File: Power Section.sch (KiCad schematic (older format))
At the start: 60 parts, among them J17 CK-JS102011SAQN, J4 USB_C_Receptacle_USB2.0, Q1 SSM6J507NU, Q2 SSM6J507NU, Q3 SSM6J507NU, Q6 SSM6J507NU, U1 LM1117LDX, U2 LDFM33PVR, U5 MCP73213, U6 BQ29209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

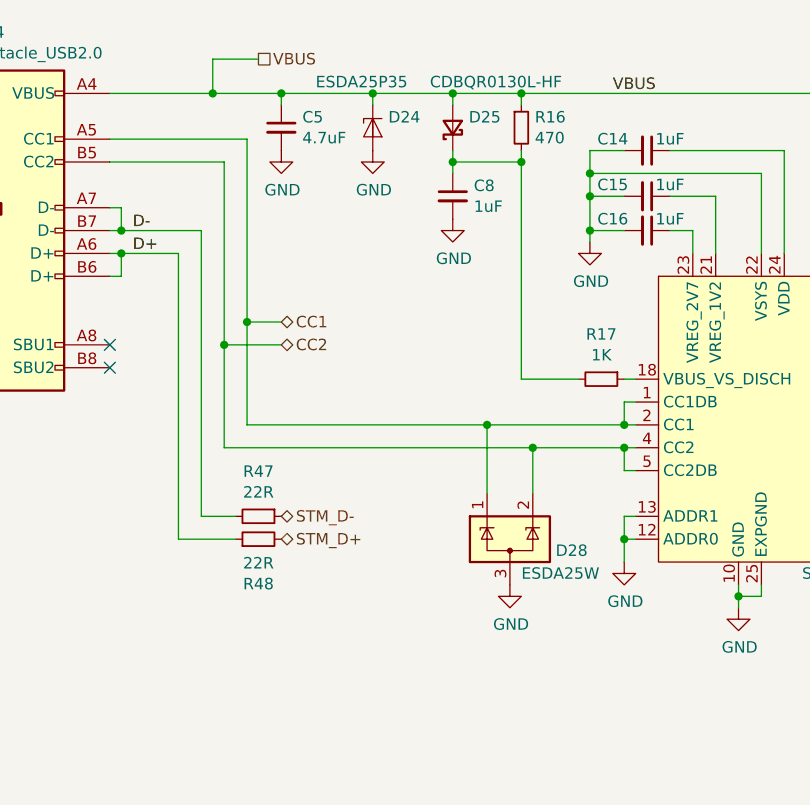
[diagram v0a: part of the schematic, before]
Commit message: Dodano projekt stacji dokującej. Poprawki ścieżek i shcematu
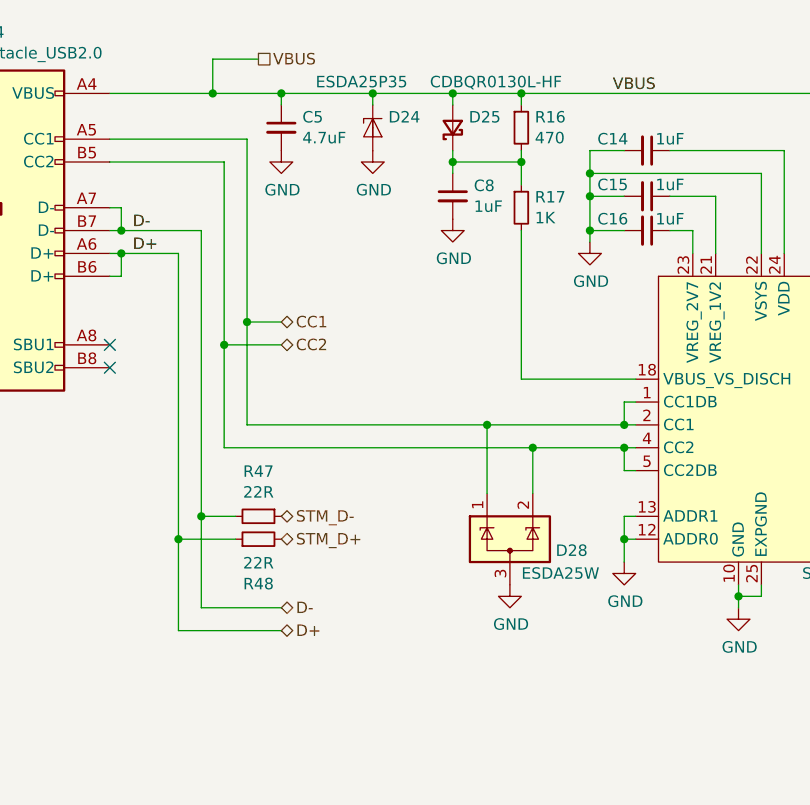
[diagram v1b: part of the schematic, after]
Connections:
- wire segments 228 -> 232
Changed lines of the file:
@@
 Connection ~ 3900 4950
-$Comp
-L Device:R_Small R17
-U 1 1 5FB18F14
-P 3800 4750
-F 0 "R17" V 3604 4750 50  0000 C CNN
-F 1 "1K" V 3695 4750 50  0000 C CNN
-F 2 "Resistor_SMD:R_0402_1005Metric" H 3800 4750 50  0001 C CNN
-F 3 "~" H 3800 4750 50  0001 C CNN
-	1    3800 4750
-	0    1    1    0
-$EndComp
-Wire Wire Line
-	3950 4750 3900 4750
 $Comp
 L Device:C_Small C16
@@
 	1    0    0    -1
 $EndComp
-Wire Wire Line
-	3700 4750 3450 4750
 $Comp
 L Device:D_Schottky_Small D25
@@
 Connection ~ 3450 3800
 Wire Wire Line
-	3450 3800 3450 4750
+	3450 3800 3450 3900
 $Comp
 L synermycha-electronics:ESDA25P35 D24
@@
 Text Label 1750 4200 0    50   ~ 0
 D+
+$Comp
+L Device:R_Small R17
+U 1 1 5FA3A7AB
+P 3450 4000
+F 0 "R17" H 3509 4046 50  0000 L CNN
+F 1 "1K" H 3509 3955 50  0000 L CNN
+F 2 "Resistor_SMD:R_0402_1005Metric" H 3450 4000 50  0001 C CNN
+F 3 "" H 3450 4000 50  0001 C CNN
+	1    3450 4000
+	1    0    0    -1
+$EndComp
+Wire Wire Line
+	3450 4100 3450 4750
+Wire Wire Line
+	3450 4750 3950 4750
+Text HLabel 2400 5750 2    50   BiDi ~ 0
+D-
+Text HLabel 2400 5850 2    50   BiDi ~ 0
+D+
+Wire Wire Line
+	2400 5750 2050 5750
+Wire Wire Line
+	2050 5750 2050 5350
+Connection ~ 2050 5350
+Wire Wire Line
+	2400 5850 1950 5850
+Wire Wire Line
+	1950 5850 1950 5450
+Connection ~ 1950 5450
 $EndSCHEMATC

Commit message: NXP version
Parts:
- removed BT2, BT3, BT4: 200mAh, Connector_PinHeader_1.27mm:PinHeader_1x02_P1.27mm_Vertical, symbol Device:Battery_Cell
- removed C14, C15, C16: 1uF, Capacitor_SMD:C_0402_1005Metric, symbol Device:C_Small
- removed C17, C18, C20, C21: 0.1uF, Capacitor_SMD:C_0402_1005Metric, symbol Device:C_Small
- removed C19: 0.33uF, Capacitor_SMD:C_0402_1005Metric, symbol Device:C_Small
- removed D25: CDBQR0130L-HF, Diode_SMD:D_0402_1005Metric, symbol Device:D_Schottky_Small
- removed D26: RED, LED_SMD:LED_0402_1005Metric, symbol Device:LED_Small
- removed D28: ESDA25W, Package_TO_SOT_SMD:SOT-323_SC-70, symbol synermycha-electronics:ESDA25W
- removed D29: ESDA25P35, footprints:1610, symbol synermycha-electronics:ESDA25P35
- removed Q2: SSM6J507NU, footprints:UDFN6B, symbol synermycha-electronics:SSM6J507NU
- removed R16: 470, Resistor_SMD:R_0402_1005Metric, symbol Device:R_Small
- removed R17: 1K, Resistor_SMD:R_0402_1005Metric, symbol Device:R_Small
- removed R18, R28: 100K, Resistor_SMD:R_0402_1005Metric, symbol Device:R_Small
- removed R21: 18K, Resistor_SMD:R_0402_1005Metric, symbol Device:R_Small
- removed R35: 100R, Resistor_SMD:R_0402_1005Metric, symbol Device:R_Small
- removed R41: 160R, Resistor_SMD:R_0402_1005Metric, symbol Device:R_Small
- removed R44: 260R, Resistor_SMD:R_0402_1005Metric, symbol Device:R_Small
- removed R45: 120R, Resistor_SMD:R_0402_1005Metric, symbol Device:R_Small
- removed R54: 2K, Resistor_SMD:R_0402_1005Metric, symbol Device:R_Small
- removed R56: 27K, Resistor_SMD:R_0402_1005Metric, symbol Device:R_Small
- removed U5: MCP73213, Package_DFN_QFN:DFN-10-1EP_3x3mm_P0.5mm_EP1.55x2.48mm, symbol synermycha-electronics:MCP73213
- removed U6: BQ29209, Package_SON:HVSON-8-1EP_3x3mm_P0.65mm_EP1.6x2.4mm, symbol synermycha-electronics:BQ29209
- removed U7: STUSB4500QTR, Package_DFN_QFN:QFN-24-1EP_4x4mm_P0.5mm_EP2.7x2.7mm, symbol synermycha-electronics:STUSB4500QTR
- added U5: SRV05-4, Package_TO_SOT_SMD:SOT-23-6, symbol Power_Protection:SRV05-4
- added U6: FUSB302BMPX, Package_DFN_QFN:WQFN-14-1EP_2.5x2.5mm_P0.5mm_EP1.45x1.45mm, symbol Interface_USB:FUSB302BMPX
- BT1: value 200mAh -> 2C, 600mAh
- C8: value 1uF -> 0.1uF
- J4: footprint Connector_USB:USB_C_Receptacle_GCT_USB4085 -> Connector_USB:USB_C_Receptacle_XKB_U262-16XN-4BVC11
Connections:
- net labels removed: VDRIVE
- wire segments 232 -> 138
- no-connect marks 14 -> 4
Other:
- note removed: "2cell balancing"
- note removed: "2cell charging"
- note removed: "Input voltage range 4 V to 10 V\nOvervoltageProtection(OVT) 4.35V\nOvervoltage detection delay time 3 s\nOvervoltage detection delay timer capacitor 0.33μF\nCell Balancing Enabled Yes\nCell Balancing Current, ICB1 and ICB2 10 mA\nCell Balancing Resistors, RCB, RCB1, RCB2 and RVD RCB= 100Ω, RCB1= 260Ω, \n RCB2= 160Ω, RVD= 100Ω"
- note removed: "Ireg = 1104 * Rprog ^ (-0.93)\nRprog in KOhm\nIreg in mAh\n1104*(27)^(-0.93) ~~= 50mA"
- note removed: "Rcb1\n"
- note removed: "Rcb2"
- note removed: "Rcb\n"
- moved on the sheet: BT1

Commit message: Back to STM, added level shifter for RGB
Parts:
- C22: footprint Capacitor_SMD:C_0805_2012Metric -> Capacitor_SMD:C_0603_1608Metric
- C6, C7, C8: footprint Capacitor_SMD:C_0402_1005Metric -> Capacitor_SMD:C_0201_0603Metric
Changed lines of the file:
@@
 F 0 "C22" H 8542 1146 50  0000 L CNN
 F 1 "100uF" H 8542 1055 50  0000 L CNN
-F 2 "Capacitor_SMD:C_0805_2012Metric" H 8450 1100 50  0001 C CNN
+F 2 "Capacitor_SMD:C_0603_1608Metric" H 8450 1100 50  0001 C CNN
 F 3 "~" H 8450 1100 50  0001 C CNN
 	1    8450 1100
@@
 F 0 "C7" H 8292 2446 50  0000 L CNN
 F 1 "1uF" H 8292 2355 50  0000 L CNN
-F 2 "Capacitor_SMD:C_0402_1005Metric" H 8200 2400 50  0001 C CNN
+F 2 "Capacitor_SMD:C_0201_0603Metric" H 8200 2400 50  0001 C CNN
 F 3 "~" H 8200 2400 50  0001 C CNN
 	1    8200 2400
@@
 F 0 "C6" H 8242 1146 50  0000 L CNN
 F 1 "1uF" H 8242 1055 50  0000 L CNN
-F 2 "Capacitor_SMD:C_0402_1005Metric" H 8150 1100 50  0001 C CNN
+F 2 "Capacitor_SMD:C_0201_0603Metric" H 8150 1100 50  0001 C CNN
 F 3 "~" H 8150 1100 50  0001 C CNN
 	1    8150 1100
@@
 F 0 "C8" H 4192 4246 50  0000 L CNN
 F 1 "0.1uF" H 4192 4155 50  0000 L CNN
-F 2 "Capacitor_SMD:C_0402_1005Metric" H 4100 4200 50  0001 C CNN
+F 2 "Capacitor_SMD:C_0201_0603Metric" H 4100 4200 50  0001 C CNN
 F 3 "~" H 4100 4200 50  0001 C CNN
 	1    4100 4200
